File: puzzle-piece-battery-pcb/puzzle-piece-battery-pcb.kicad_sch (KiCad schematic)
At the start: 18 parts, among them J1 Lipo, J2 INPUT, J3 OUTPUT, J4 GND Rivet, J5 5V Rivet, J6 3.3V Rivet, U2 MCP73831T-2ACI/OT, U3 LM3480-3.3

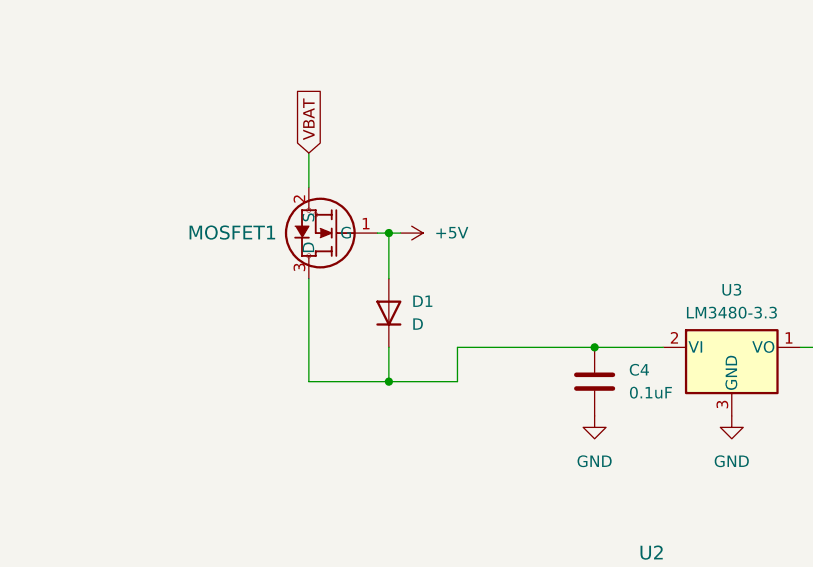
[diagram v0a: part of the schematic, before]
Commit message: fixed transistor in battery pcb
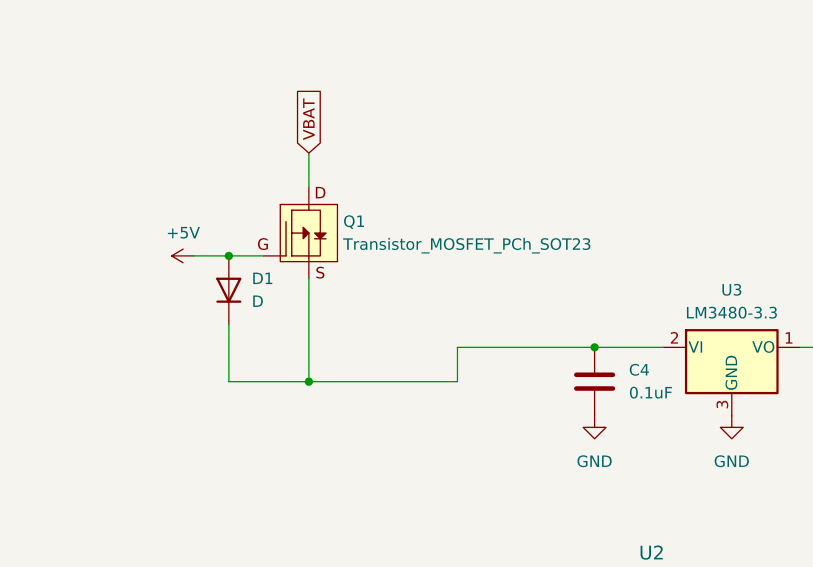
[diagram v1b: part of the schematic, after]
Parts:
- removed MOSFET1: ZXM61P03FTA, ZXM61P03FTA:SOT23_ZETEX_DIO, symbol ZXM61P03FTA:ZXM61P03FTA
- added Q1: Transistor_MOSFET_PCh_SOT23, fab:SOT-23-3, symbol fab:Transistor_MOSFET_PCh_SOT23
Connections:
- net +5V: now also Q1.1 (G)
- net VBAT: now also Q1.3 (D)
- net at C4.1, D1.1 (K), U3.2 (VI): now also Q1.2 (S)
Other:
- moved on the sheet: D1
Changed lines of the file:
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@@
-	)
-	(junction
-		(at 101.6 66.04)
-		(diameter 0)
-		(color 0 0 0 0)
 	)
 	(junction
@@
 	)
 	(junction
-		(at 101.6 82.55)
+		(at 83.82 68.58)
 		(diameter 0)
 		(color 0 0 0 0)
@@
 	)
 	(junction
+		(at 92.71 82.55)
+		(diameter 0)
+		(color 0 0 0 0)
+	)
+	(junction
 		(at 167.64 124.46)
 		(diameter 0)
@@
 	(wire
 		(pts
-			(xy 101.6 66.04) (xy 101.6 71.12)
-		)
-		(stroke
-			(width 0)
-			(type default)
-		)
-	)
-	(wire
-		(pts
 			(xy 190.5 113.03) (xy 199.39 113.03)
 		)
@@
 	(wire
 		(pts
+			(xy 83.82 82.55) (xy 92.71 82.55)
+		)
+		(stroke
+			(width 0)
+			(type default)
+		)
+	)
+	(wire
+		(pts
 			(xy 187.96 114.3) (xy 189.23 114.3)
 		)
@@
 	(wire
 		(pts
-			(xy 100.33 66.04) (xy 101.6 66.04)
-		)
-		(stroke
-			(width 0)
-			(type default)
-		)
-	)
-	(wire
-		(pts
 			(xy 161.29 124.46) (xy 162.56 124.46)
 		)
@@
 	(wire
 		(pts
-			(xy 101.6 78.74) (xy 101.6 82.55)
-		)
-		(stroke
-			(width 0)
-			(type default)
-		)
-	)
-	(wire
-		(pts
 			(xy 190.5 120.65) (xy 196.85 120.65)
 		)
@@
 	(wire
 		(pts
+			(xy 83.82 76.2) (xy 83.82 82.55)
+		)
+		(stroke
+			(width 0)
+			(type default)
+		)
+	)
+	(wire
+		(pts
 			(xy 124.46 78.74) (xy 109.22 78.74)
 		)
@@
 	(wire
 		(pts
-			(xy 92.71 82.55) (xy 101.6 82.55)
+			(xy 83.82 68.58) (xy 87.63 68.58)
+		)
+		(stroke
+			(width 0)
+			(type default)
+		)
+	)
+	(wire
+		(pts
+			(xy 92.71 82.55) (xy 109.22 82.55)
 		)
 		(stroke
@@
 	(wire
 		(pts
-			(xy 101.6 66.04) (xy 102.87 66.04)
-		)
-		(stroke
-			(width 0)
-			(type default)
-		)
-	)
-	(wire
-		(pts
 			(xy 161.29 114.3) (xy 187.96 114.3)
 		)
@@
 	(wire
 		(pts
-			(xy 109.22 82.55) (xy 101.6 82.55)
+			(xy 80.01 68.58) (xy 83.82 68.58)
 		)
 		(stroke
@@
 	(symbol
 		(lib_id "power:+5V")
-		(at 102.87 66.04 270)
+		(at 80.01 68.58 90)
 		(unit 1)
 		(exclude_from_sim no)
@@
 		(fields_autoplaced yes)
 		(property "Reference" "#PWR05"
-			(at 99.06 66.04 0)
+			(at 83.82 68.58 0)
 			(effects
 				(font
@@
 		)
 		(property "Value" "+5V"
-			(at 106.68 66.0399 90)
-			(effects
-				(font
-					(size 1.27 1.27)
-				)
-				(justify left)
+			(at 78.74 66.04 90)
+			(effects
+				(font
+					(size 1.27 1.27)
+				)
 			)
 		)
 		(property "Footprint" ""
-			(at 102.87 66.04 0)
+			(at 80.01 68.58 0)
 			(effects
 				(font
@@
 		)
 		(property "Datasheet" ""
-			(at 102.87 66.04 0)
+			(at 80.01 68.58 0)
 			(effects
 				(font
@@
 		)
 		(property "Description" "Power symbol creates a global label with name \"+5V\""
-			(at 102.87 66.04 0)
+			(at 80.01 68.58 0)
 			(effects
 				(font
@@
 	(symbol
 		(lib_id "Device:D")
-		(at 101.6 74.93 90)
-		(unit 1)
-		(exclude_from_sim no)
-		(in_bom yes)
-		(on_board yes)
-		(dnp no)
-		(fields_autoplaced yes)
+		(at 83.82 72.39 90)
+		(unit 1)
+		(exclude_from_sim no)
+		(in_bom yes)
+		(on_board yes)
+		(dnp no)
 		(property "Reference" "D1"
-			(at 104.14 73.6599 90)
+			(at 86.36 71.1199 90)
 			(effects
 				(font
@@
 		)
 		(property "Value" "D"
-			(at 104.14 76.1999 90)
+			(at 86.36 73.6599 90)
 			(effects
 				(font
@@
 		)
 		(property "Footprint" "Diode_SMD:D_1206_3216Metric_Pad1.42x1.75mm_HandSolder"
-			(at 101.6 74.93 0)
+			(at 83.82 72.39 0)
 			(effects
 				(font
@@
 		)
 		(property "Datasheet" "~"
-			(at 101.6 74.93 0)
+			(at 83.82 72.39 0)
 			(effects
 				(font
@@
 		)
 		(property "Description" "Diode"
-			(at 101.6 74.93 0)
+			(at 83.82 72.39 0)
 			(effects
 				(font
@@
 		)
 		(property "Sim.Device" "D"
-			(at 101.6 74.93 0)
+			(at 83.82 72.39 0)
 			(effects
 				(font
@@
 		)
 		(property "Sim.Pins" "1=K 2=A"
-			(at 101.6 74.93 0)
+			(at 83.82 72.39 0)
 			(effects
 				(font
@@
 	)
 	(symbol
+		(lib_id "fab:Transistor_MOSFET_PCh_SOT23")
+		(at 92.71 66.04 0)
+		(unit 1)
+		(exclude_from_sim no)
+		(in_bom yes)
+		(on_board yes)
+		(dnp no)
+		(fields_autoplaced yes)
+		(property "Reference" "Q1"
+			(at 96.52 64.7699 0)
+			(effects
+				(font
+					(size 1.27 1.27)
+				)
+				(justify left)
+			)
+		)
+		(property "Value" "Transistor_MOSFET_PCh_SOT23"
+			(at 96.52 67.3099 0)
+			(effects
+				(font
+					(size 1.27 1.27)
+				)
+				(justify left)
+			)
+		)
+		(property "Footprint" "fab:SOT-23-3"
+			(at 92.71 66.04 0)
+			(effects
+				(font
+					(size 1.27 1.27)
+				)
+				(hide yes)
+			)
+		)
+		(property "Datasheet" "https://www.onsemi.com/pub/Collateral/NDS356AP-D.PDF"
+			(at 92.71 66.04 0)
+			(effects
+				(font
+					(size 1.27 1.27)
+				)
+				(hide yes)
+			)
+		)
+		(property "Description" "P-Channel mosfet NDS356AP in SOT-23 package"
+			(at 92.71 66.04 0)
+			(effects
+				(font
+					(size 1.27 1.27)
+				)
+				(hide yes)
+			)
+		)
+		(pin "3"
+		)
+		(pin "1"
+		)
+		(pin "2"
+		)
+		(instances
+			(project ""
+				(path "/ec51d40a-bf9e-4672-a46c-de32b19bd793"
+					(reference "Q1")
+					(unit 1)
+				)
+			)
+		)
+	)
+	(symbol
 		(lib_id "power:+3.3V")
 		(at 160.02 78.74 270)
@@
 					(unit 1)
 				)
-			)
-		)
-	)
-	(symbol
-		(lib_id "ZXM61P03FTA:ZXM61P03FTA")
-		(at 100.33 66.04 180)
-		(unit 1)
-		(exclude_from_sim no)
-		(in_bom yes)
-		(on_board yes)
-		(dnp no)
-		(property "Reference" "MOSFET1"
-			(at 89.154 66.04 0)
-			(effects
-				(font
-					(size 1.524 1.524)
-				)
-				(justify left)
-			)
-		)
-		(property "Value" "ZXM61P03FTA"
-			(at 88.9 64.7701 0)
-			(effects
-				(font
-					(size 1.524 1.524)
-				)
-				(justify left)
-				(hide yes)
-			)
-		)
-		(property "Footprint" "ZXM61P03FTA:SOT23_ZETEX_DIO"
-			(at 100.33 66.04 0)
-			(effects
-				(font
-					(size 1.27 1.27)
-					(italic yes)
-				)
-				(hide yes)
-			)
-		)
-		(property "Datasheet" "ZXM61P03FTA"
-			(at 100.33 66.04 0)
-			(effects
-				(font
-					(size 1.27 1.27)
-					(italic yes)
-				)
-				(hide yes)
-			)
-		)
-		(property "Description" ""
-			(at 100.33 66.04 0)
-			(effects
-				(font
-					(size 1.27 1.27)
-				)
-				(hide yes)
-			)
-		)
-		(pin "2"
-		)
-		(pin "3"
-		)
-		(pin "1"
-		)
-		(instances
-			(project ""
-				(path "/ec51d40a-bf9e-4672-a46c-de32b19bd793"
-					(reference "MOSFET1")
-					(unit 1)
-				)
